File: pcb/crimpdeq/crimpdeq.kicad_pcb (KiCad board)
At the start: 2 copper layers, 23 x 63.8 mm, 48 parts, among them J2 USB4105-GF-A, J3 Loadcell_Pads, J4 Power_Sense_Pads, Q1 SS8550, Q2 DMG3415U, U1 ESP32-C3-MINI-1, U2 MCP73831T-2ACI/OT, U3 HX711, U5 MAX17048G+T10, U6 SY8088

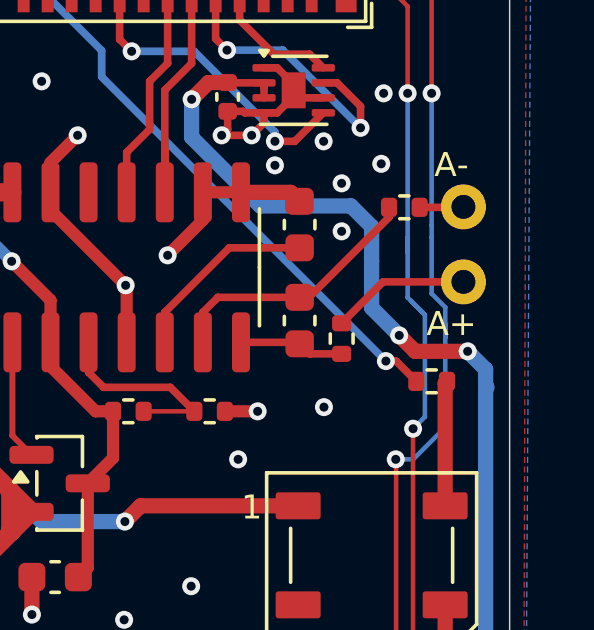
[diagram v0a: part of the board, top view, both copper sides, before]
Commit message: fix: Remove unused tracks
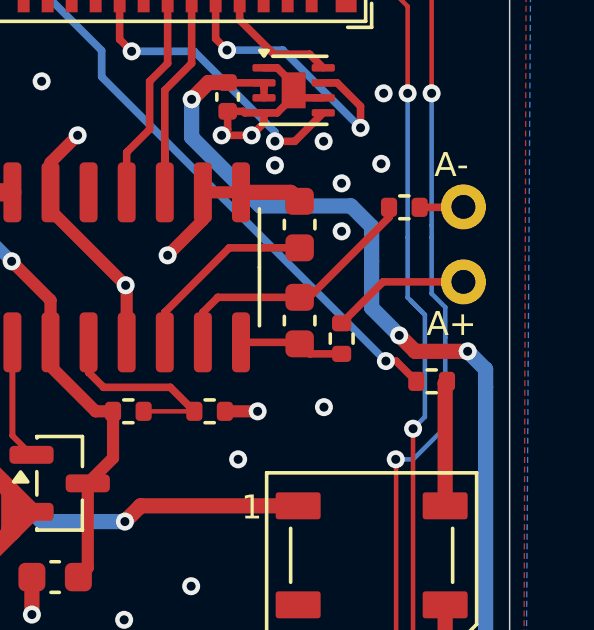
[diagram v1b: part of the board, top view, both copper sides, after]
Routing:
- net USB_D-: track 54.6 -> 54.1 mm
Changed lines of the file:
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@@
 	)
 	(segment
-		(start 150.054 74.54)
-		(end 150.054 74.08931)
-		(width 0.1524)
-		(layer "B.Cu")
-		(net "USB_D+")
-	)
-	(segment
 		(start 149.6 73.076266)
 		(end 149.6 71.2)
@@
 	)
 	(segment
-		(start 151.4 76.2)
-		(end 151.446 76.2)
-		(width 0.508)
-		(layer "B.Cu")
-		(net "+BATT")
-	)
-	(segment
 		(start 149.6 100.185)
 		(end 151.4 98.385)
@@
 		(width 0.1524)
 		(layer "B.Cu")
-		(net "USB_D-")
-	)
-	(segment
-		(start 148.8 71.2)
-		(end 148.8 71.7)
-		(width 0.1524)
-		(layer "B.Cu")
